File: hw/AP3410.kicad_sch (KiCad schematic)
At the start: 6 parts

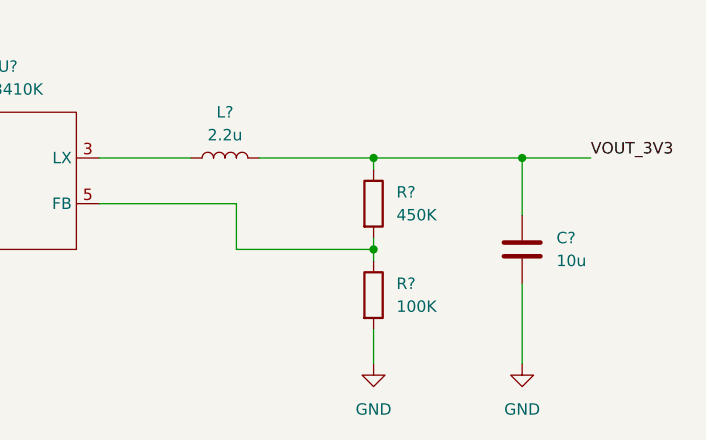
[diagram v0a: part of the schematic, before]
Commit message: setup components information
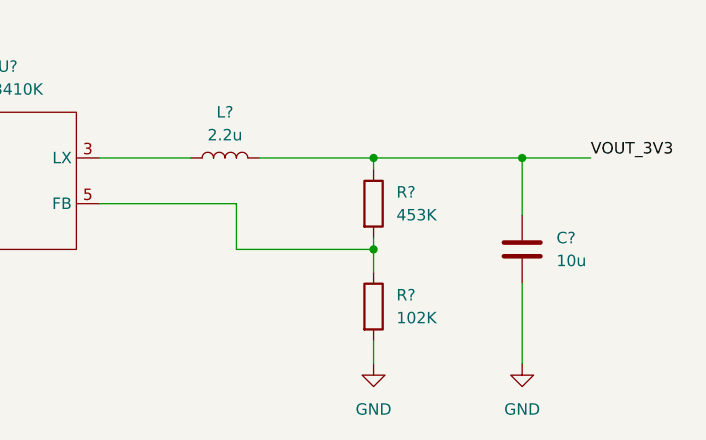
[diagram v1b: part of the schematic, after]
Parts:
- C?: footprint (none) -> Capacitor_SMD:C_0805_2012Metric_Pad1.18x1.45mm_HandSolder; LCSC (none) -> C1779; Vendor (none) -> SAMSUNG(三星); Vendor Model (none) -> CL21A475KAQNNNE
- C?: footprint (none) -> Capacitor_SMD:C_0805_2012Metric_Pad1.18x1.45mm_HandSolder; LCSC (none) -> C15850; Vendor (none) -> SAMSUNG(三星); Vendor Model (none) -> CL21A106KAYNNNE
- L?: footprint (none) -> Inductor_SMD:L_Sunlord_SWPA3015S; LCSC (none) -> C19734; Vendor (none) -> Sunlord(顺络); Vendor Model (none) -> SWPA3015S2R2NT
- R?: value 450K -> 453K; footprint (none) -> Resistor_SMD:R_0805_2012Metric_Pad1.20x1.40mm_HandSolder; LCSC (none) -> C204515; Vendor (none) -> BOURNS; Vendor Model (none) -> CR0805-FX-4533ELF
- R?: value 100K -> 102K; footprint (none) -> Resistor_SMD:R_0805_2012Metric_Pad1.20x1.40mm_HandSolder; LCSC (none) -> C228247; Vendor (none) -> YAGEO(国巨); Vendor Model (none) -> AC0805FR-07102KL
- U?: LCSC (none) -> C82763; Vendor (none) -> DIODES(美台); Vendor Model (none) -> AP3410KTR-G1
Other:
- moved on the sheet: R?
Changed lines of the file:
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@@
     (stroke (width 0) (type default))
   )
-  (wire (pts (xy 152.4 76.2) (xy 152.4 77.47))
+  (wire (pts (xy 152.4 76.2) (xy 152.4 78.74))
     (stroke (width 0) (type default))
   )
@@
     (stroke (width 0) (type default))
   )
-  (wire (pts (xy 152.4 85.09) (xy 152.4 88.9))
+  (wire (pts (xy 152.4 86.36) (xy 152.4 88.9))
     (stroke (width 0) (type default))
   )
@@
     )
     (property "Datasheet" "https://www.diodes.com/assets/Datasheets/products_inactive_data/AP3410.pdf" (at 111.76 81.28 0)
+      (effects (font (size 1.27 1.27)) hide)
+    )
+    (property "Description" "功能类型: 降压型 同步整流: 是 输出类型: 可调 输出通道数: 1 拓扑结构: 降压式 输入电压: 2.5V~5.5V 输出电压:" (at 111.76 68.58 0)
+      (effects (font (size 1.27 1.27)) hide)
+    )
+    (property "LCSC" "C82763" (at 111.76 68.58 0)
+      (effects (font (size 1.27 1.27)) hide)
+    )
+    (property "Vendor" "DIODES(美台)" (at 111.76 68.58 0)
+      (effects (font (size 1.27 1.27)) hide)
+    )
+    (property "Vendor Model" "AP3410KTR-G1" (at 111.76 68.58 0)
       (effects (font (size 1.27 1.27)) hide)
     )
@@
       (effects (font (size 1.27 1.27)) (justify left))
     )
-    (property "Footprint" "" (at 79.7052 77.47 0)
+    (property "Footprint" "Capacitor_SMD:C_0805_2012Metric_Pad1.18x1.45mm_HandSolder" (at 79.7052 77.47 0)
       (effects (font (size 1.27 1.27)) hide)
     )
@@
       (effects (font (size 1.27 1.27)) hide)
     )
+    (property "Description" "容值: 4.7uF 精度: ±10% 额定电压: 25V 材质(温度系数): X5R 材质:X5R" (at 78.74 73.66 0)
+      (effects (font (size 1.27 1.27)) hide)
+    )
+    (property "LCSC" "C1779" (at 78.74 73.66 0)
+      (effects (font (size 1.27 1.27)) hide)
+    )
+    (property "Vendor" "SAMSUNG(三星)" (at 78.74 73.66 0)
+      (effects (font (size 1.27 1.27)) hide)
+    )
+    (property "Vendor Model" "CL21A475KAQNNNE" (at 78.74 73.66 0)
+      (effects (font (size 1.27 1.27)) hide)
+    )
     (pin "1")
     (pin "2")
@@
       (effects (font (size 1.27 1.27)) (justify left))
     )
-    (property "Value" "450K" (at 154.94 72.39 0)
-      (effects (font (size 1.27 1.27)) (justify left))
-    )
-    (property "Footprint" "" (at 150.622 71.12 90)
+    (property "Value" "453K" (at 154.94 72.39 0)
+      (effects (font (size 1.27 1.27)) (justify left))
+    )
+    (property "Footprint" "Resistor_SMD:R_0805_2012Metric_Pad1.20x1.40mm_HandSolder" (at 150.622 71.12 90)
       (effects (font (size 1.27 1.27)) hide)
     )
@@
       (effects (font (size 1.27 1.27)) hide)
     )
+    (property "Description" "电阻类型: 厚膜电阻 阻值: 453kΩ 精度: ±1% 功率: 0.125W 温度系数: ±100ppm/℃ 工作温度范围: -55℃~+155℃" (at 152.4 71.12 0)
+      (effects (font (size 1.27 1.27)) hide)
+    )
+    (property "LCSC" "C204515" (at 152.4 71.12 0)
+      (effects (font (size 1.27 1.27)) hide)
+    )
+    (property "Vendor" "BOURNS" (at 152.4 71.12 0)
+      (effects (font (size 1.27 1.27)) hide)
+    )
+    (property "Vendor Model" "CR0805-FX-4533ELF" (at 152.4 71.12 0)
+      (effects (font (size 1.27 1.27)) hide)
+    )
     (pin "1")
     (pin "2")
@@
       (effects (font (size 1.27 1.27)))
     )
-    (property "Footprint" "" (at 135.89 66.04 0)
+    (property "Footprint" "Inductor_SMD:L_Sunlord_SWPA3015S" (at 135.89 66.04 0)
       (effects (font (size 1.27 1.27)) hide)
     )
@@
       (effects (font (size 1.27 1.27)) hide)
     )
+    (property "Description" "电感值:2.2uH,直流电阻(DCR):78mΩ,类型:-,精度:±30%,车规等级:-,额定电流:1.6A,饱和电流(Isat):2A" (at 135.89 66.04 0)
+      (effects (font (size 1.27 1.27)) hide)
+    )
+    (property "LCSC" "C19734" (at 135.89 66.04 0)
+      (effects (font (size 1.27 1.27)) hide)
+    )
+    (property "Vendor" "Sunlord(顺络)" (at 135.89 66.04 0)
+      (effects (font (size 1.27 1.27)) hide)
+    )
+    (property "Vendor Model" "SWPA3015S2R2NT" (at 135.89 66.04 0)
+      (effects (font (size 1.27 1.27)) hide)
+    )
     (pin "1")
     (pin "2")
@@
     )
   )
-  (symbol (lib_id "Device:R") (at 152.4 81.28 0) (unit 1)
-    (in_bom yes) (on_board yes) (dnp no) (fields_autoplaced)
-    (property "Reference" "R?" (at 154.94 80.01 0)
-      (effects (font (size 1.27 1.27)) (justify left))
-    )
-    (property "Value" "100K" (at 154.94 82.55 0)
-      (effects (font (size 1.27 1.27)) (justify left))
-    )
-    (property "Footprint" "" (at 150.622 81.28 90)
-      (effects (font (size 1.27 1.27)) hide)
-    )
-    (property "Datasheet" "~" (at 152.4 81.28 0)
+  (symbol (lib_id "Device:R") (at 152.4 82.55 0) (unit 1)
+    (in_bom yes) (on_board yes) (dnp no) (fields_autoplaced)
+    (property "Reference" "R?" (at 154.94 81.28 0)
+      (effects (font (size 1.27 1.27)) (justify left))
+    )
+    (property "Value" "102K" (at 154.94 83.82 0)
+      (effects (font (size 1.27 1.27)) (justify left))
+    )
+    (property "Footprint" "Resistor_SMD:R_0805_2012Metric_Pad1.20x1.40mm_HandSolder" (at 150.622 82.55 90)
+      (effects (font (size 1.27 1.27)) hide)
+    )
+    (property "Datasheet" "~" (at 152.4 82.55 0)
+      (effects (font (size 1.27 1.27)) hide)
+    )
+    (property "Description" "电阻类型: 厚膜电阻 阻值: 102kΩ 精度: ±1% 功率: 125mW 温度系数: ±100ppm/℃ 最大工作电压: 150V 工作温" (at 152.4 82.55 0)
+      (effects (font (size 1.27 1.27)) hide)
+    )
+    (property "LCSC" "C228247" (at 152.4 82.55 0)
+      (effects (font (size 1.27 1.27)) hide)
+    )
+    (property "Vendor" "YAGEO(国巨)" (at 152.4 82.55 0)
+      (effects (font (size 1.27 1.27)) hide)
+    )
+    (property "Vendor Model" "AC0805FR-07102KL" (at 152.4 82.55 0)
       (effects (font (size 1.27 1.27)) hide)
     )
@@
       (effects (font (size 1.27 1.27)) (justify left))
     )
-    (property "Footprint" "" (at 169.8752 80.01 0)
+    (property "Footprint" "Capacitor_SMD:C_0805_2012Metric_Pad1.18x1.45mm_HandSolder" (at 169.8752 80.01 0)
       (effects (font (size 1.27 1.27)) hide)
     )
@@
       (effects (font (size 1.27 1.27)) hide)
     )
+    (property "Description" "容值: 10uF 精度: ±10% 额定电压: 25V 材质(温度系数): X5R 材质:X5R 每盘2000个 7''REEL" (at 168.91 76.2 0)
+      (effects (font (size 1.27 1.27)) hide)
+    )
+    (property "LCSC" "C15850" (at 168.91 76.2 0)
+      (effects (font (size 1.27 1.27)) hide)
+    )
+    (property "Vendor" "SAMSUNG(三星)" (at 168.91 76.2 0)
+      (effects (font (size 1.27 1.27)) hide)
+    )
+    (property "Vendor Model" "CL21A106KAYNNNE" (at 168.91 76.2 0)
+      (effects (font (size 1.27 1.27)) hide)
+    )

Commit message: annotations
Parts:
- gave numbers to parts that had none: 6
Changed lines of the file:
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@@
   (symbol (lib_id "IotPi_Regulator_Switching:AP3410K") (at 111.76 68.58 0) (unit 1)
     (in_bom yes) (on_board yes) (dnp no) (fields_autoplaced)
-    (property "Reference" "U?" (at 111.76 55.88 0)
+    (property "Reference" "U4" (at 111.76 55.88 0)
       (effects (font (size 1.27 1.27)))
     )
@@
       (project "KiConSZ2023"
         (path "/8659c260-f029-4e72-8b9a-85fff45eea40/f453823a-a381-482a-9343-94fafcdcaf18/a840a96c-0798-4e19-9437-8cd8130a96d6"
-          (reference "U?") (unit 1)
+          (reference "U4") (unit 1)
         )
       )
@@
   (symbol (lib_id "power:GND") (at 152.4 88.9 0) (unit 1)
     (in_bom yes) (on_board yes) (dnp no) (fields_autoplaced)
-    (property "Reference" "#PWR?" (at 152.4 95.25 0)
+    (property "Reference" "#PWR012" (at 152.4 95.25 0)
       (effects (font (size 1.27 1.27)) hide)
     )
@@
       (project "KiConSZ2023"
         (path "/8659c260-f029-4e72-8b9a-85fff45eea40/f453823a-a381-482a-9343-94fafcdcaf18/a840a96c-0798-4e19-9437-8cd8130a96d6"
-          (reference "#PWR?") (unit 1)
+          (reference "#PWR012") (unit 1)
         )
       )
@@
   (symbol (lib_id "Device:C") (at 78.74 73.66 0) (unit 1)
     (in_bom yes) (on_board yes) (dnp no) (fields_autoplaced)
-    (property "Reference" "C?" (at 82.55 72.39 0)
+    (property "Reference" "C10" (at 82.55 72.39 0)
       (effects (font (size 1.27 1.27)) (justify left))
     )
@@
       (project "KiConSZ2023"
         (path "/8659c260-f029-4e72-8b9a-85fff45eea40/f453823a-a381-482a-9343-94fafcdcaf18/a840a96c-0798-4e19-9437-8cd8130a96d6"
-          (reference "C?") (unit 1)
+          (reference "C10") (unit 1)
         )
       )
@@
   (symbol (lib_id "Device:R") (at 152.4 71.12 0) (unit 1)
     (in_bom yes) (on_board yes) (dnp no) (fields_autoplaced)
-    (property "Reference" "R?" (at 154.94 69.85 0)
+    (property "Reference" "R150" (at 154.94 69.85 0)
       (effects (font (size 1.27 1.27)) (justify left))
     )
@@
       (project "KiConSZ2023"
         (path "/8659c260-f029-4e72-8b9a-85fff45eea40/f453823a-a381-482a-9343-94fafcdcaf18/a840a96c-0798-4e19-9437-8cd8130a96d6"
-          (reference "R?") (unit 1)
+          (reference "R150") (unit 1)
         )
       )
@@
   (symbol (lib_id "power:GND") (at 78.74 83.82 0) (unit 1)
     (in_bom yes) (on_board yes) (dnp no) (fields_autoplaced)
-    (property "Reference" "#PWR?" (at 78.74 90.17 0)
+    (property "Reference" "#PWR011" (at 78.74 90.17 0)
       (effects (font (size 1.27 1.27)) hide)
     )
@@
       (project "KiConSZ2023"
         (path "/8659c260-f029-4e72-8b9a-85fff45eea40/f453823a-a381-482a-9343-94fafcdcaf18/a840a96c-0798-4e19-9437-8cd8130a96d6"
-          (reference "#PWR?") (unit 1)
+          (reference "#PWR011") (unit 1)
         )
       )
@@
   (symbol (lib_id "Device:L") (at 135.89 66.04 90) (unit 1)
     (in_bom yes) (on_board yes) (dnp no) (fields_autoplaced)
-    (property "Reference" "L?" (at 135.89 60.96 90)
+    (property "Reference" "L2" (at 135.89 60.96 90)
       (effects (font (size 1.27 1.27)))
     )
@@
       (project "KiConSZ2023"
         (path "/8659c260-f029-4e72-8b9a-85fff45eea40/f453823a-a381-482a-9343-94fafcdcaf18/a840a96c-0798-4e19-9437-8cd8130a96d6"
-          (reference "L?") (unit 1)
+          (reference "L2") (unit 1)
         )
       )
@@
   (symbol (lib_id "Device:R") (at 152.4 82.55 0) (unit 1)
     (in_bom yes) (on_board yes) (dnp no) (fields_autoplaced)
-    (property "Reference" "R?" (at 154.94 81.28 0)
+    (property "Reference" "R151" (at 154.94 81.28 0)
       (effects (font (size 1.27 1.27)) (justify left))
     )
@@
       (project "KiConSZ2023"
         (path "/8659c260-f029-4e72-8b9a-85fff45eea40/f453823a-a381-482a-9343-94fafcdcaf18/a840a96c-0798-4e19-9437-8cd8130a96d6"
-          (reference "R?") (unit 1)
+          (reference "R151") (unit 1)
         )
       )
@@
   (symbol (lib_id "power:GND") (at 168.91 88.9 0) (unit 1)
     (in_bom yes) (on_board yes) (dnp no) (fields_autoplaced)
-    (property "Reference" "#PWR?" (at 168.91 95.25 0)
+    (property "Reference" "#PWR013" (at 168.91 95.25 0)
       (effects (font (size 1.27 1.27)) hide)
     )
@@
       (project "KiConSZ2023"
         (path "/8659c260-f029-4e72-8b9a-85fff45eea40/f453823a-a381-482a-9343-94fafcdcaf18/a840a96c-0798-4e19-9437-8cd8130a96d6"
-          (reference "#PWR?") (unit 1)
+          (reference "#PWR013") (unit 1)
         )
       )
@@
   (symbol (lib_id "Device:C") (at 168.91 76.2 0) (unit 1)
     (in_bom yes) (on_board yes) (dnp no) (fields_autoplaced)
-    (property "Reference" "C?" (at 172.72 74.93 0)
+    (property "Reference" "C11" (at 172.72 74.93 0)
       (effects (font (size 1.27 1.27)) (justify left))
     )
@@
       (project "KiConSZ2023"
         (path "/8659c260-f029-4e72-8b9a-85fff45eea40/f453823a-a381-482a-9343-94fafcdcaf18/a840a96c-0798-4e19-9437-8cd8130a96d6"
-          (reference "C?") (unit 1)
-        )
-      )
+          (reference "C11") (unit 1)
+        )
+      )
